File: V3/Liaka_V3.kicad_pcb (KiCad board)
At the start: 4 copper layers, 101.6 x 26.9 mm, 81 parts, among them IC1 XTSD04GLGEAG, J1 Conn_Coaxial, J2 2-3S_LiPo_LARGE_HOLE_XT-30, J3 RRC3_In, J4 I2C_Interface_Male, J5 USB_B_Micro, J7 THD2528-11SD-GF, Q1 Si2301CDS, Q2 Si2301CDS, Q3 Si2301CDS, Q4 MMBT2222, Q5 MMBT2222, Q6 2N7002, SW1 SW_SPDT, SW2 RST, SW3 BOOT, SW4 SD_DUMP, U1 L80-M39, U10 MPU-6050, U2 MS561101BA03-50, U3 ADXL375BCCZ-RL7, U4 RFM95W-915S2, U5 LM393, U6 ADR5040ARTZ-2.048, U7 AMS1117-3.3, U8 CP2102N-A01-GQFN28, U9 ESP32-WROOM-32

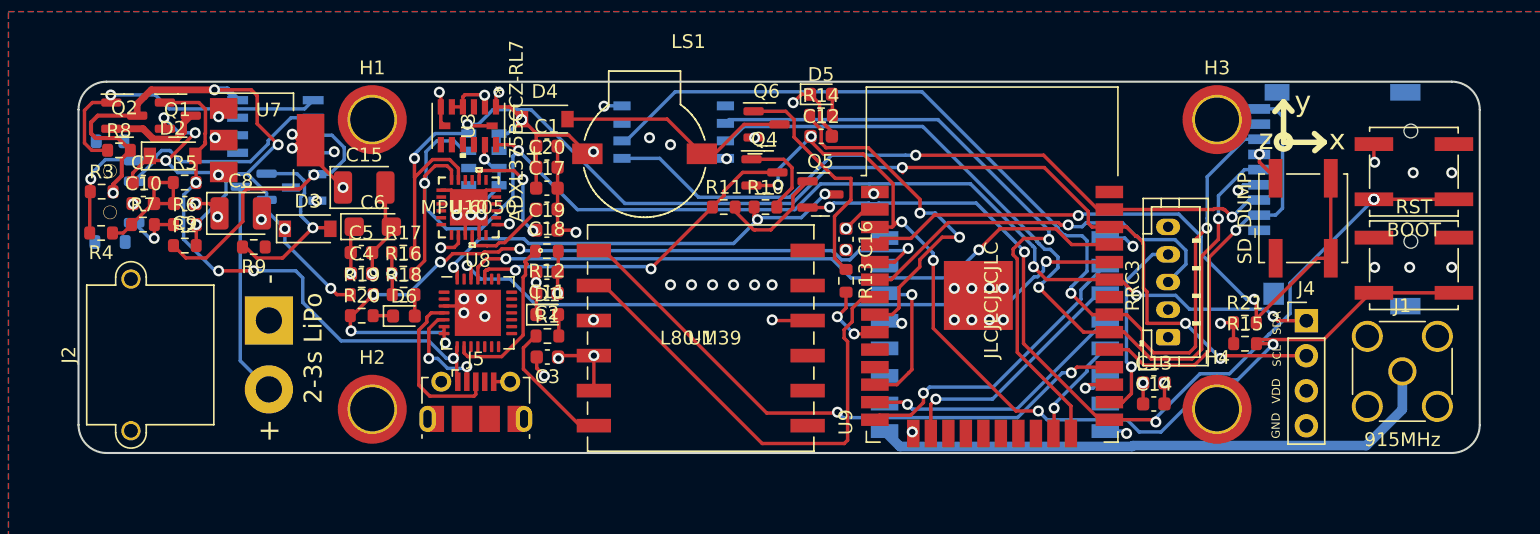
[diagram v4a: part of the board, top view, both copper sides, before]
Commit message: New parts placed and routed
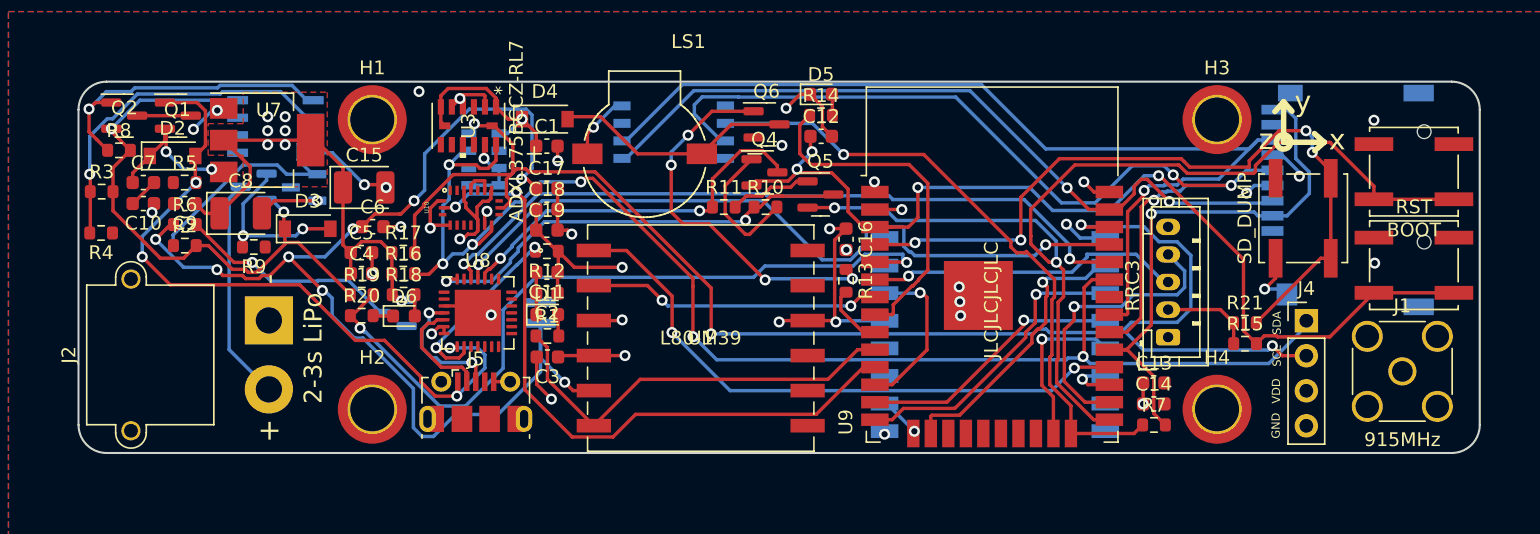
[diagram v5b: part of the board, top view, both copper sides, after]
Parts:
- removed C20: 0.1uF, Capacitor_SMD:C_0603_1608Metric
- removed SW1: SW_SPDT, Local_footprints:SSSS811101
- added BT1: MS621FE-FL11E, Local_footprints:BAT_MS621FE-FL11E, B.Cu at (135.1, 98.0)
- added D7: BAT54C, Package_TO_SOT_SMD:SOT-23, B.Cu at (129.5, 98.0)
- C17: value 10nF -> 4.7u
- C18: value 0.1uF -> 100nF
- C19: value 2.2nF -> 100nF
- C6: value 10uF -> 100n; footprint Capacitor_Tantalum_SMD:CP_EIA-3216-18_Kemet-A -> Capacitor_SMD:C_0603_1608Metric
- R2: value 50k -> 56k
- R6: value 3M -> 1k
- R7: value 1M -> NC
- U10: value MPU-6050 -> BMX055; footprint Local_footprints:MPU-6050 -> Local_footprints:BMX055
- moved R7 74.7 mm to (184.7, 106.2)
- moved J7 0.97 mm to (201.0, 90.1)
- moved U10 0.15 mm to (135.1, 90.4), turned to 90 degrees
- turned C10 to 180 degrees
- turned C18 to 0 degrees
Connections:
- net BOOT renamed /BOOT
- net BUZZER renamed /ESP32/BUZZER
- net Batt_sense renamed /ESP32/Batt_sense
- net CLK_SD renamed /CLK_SD
- net CS_RF renamed /CS_RF
- net DTR renamed /Programming/DTR
- net EN renamed /EN
- net ESP_LED renamed /ESP32/ESP_LED
- net MISO_SD renamed /MISO_SD
- net MOSI_SD renamed /MOSI_SD
- net RESET_RF renamed /RESET_RF
- net RF_IO0 renamed /RF_IO0
- net RTS renamed /Programming/RTS
- net RXD0 renamed /RXD0
- net RXD1_RRC3 renamed /RXD1_RRC3
- net RXD2_GPS renamed /RXD2_GPS
- net SCK_RF renamed /SCK_RF
- net SD_DUMP renamed /SD_DUMP
- net TXD0 renamed /TXD0
- net TXD1_RRC3 renamed /TXD1_RRC3
- net TXD2_GPS renamed /TXD2_GPS
- C17 pad 1: VDD -> /Sensors/V_BKCP
- C18 pad 1: GND -> VDD
- C18 pad 2: Net-(C18-Pad2) -> GND
- C19 pad 1: Net-(C19-Pad1) -> VDD
- C6 pad 1: VDD -> /Sensors/V_BKCP
- IC1 pad 2: CS_XT -> /CS_XT
- J4 pad 1: SDA -> /SDA
- J4 pad 2: SCL -> /SCL
- J7 pad 2: CS_SD -> /CS_SD
- J7 pad 9: CS_SD -> /CS_SD
- J7 pad MP1: unconnected-(J7-PadMP1) -> GND
- J7 pad MP2: unconnected-(J7-PadMP2) -> GND
- J7 pad MP3: unconnected-(J7-PadMP3) -> GND
- J7 pad MP4: unconnected-(J7-PadMP4) -> GND
- Q2 pad 2: VCC -> VDC
- Q2 pad 3: VDC -> VCC
- R1 pad 1: Net-(R1-Pad1) -> /GPS_PPS
- R16 pad 2: SDA -> /SDA
- R17 pad 2: SCL -> /SCL
- R3 pad 1: /Power/2s -> Net-(R3-Pad1)
- R4 pad 2: /Power/2s -> Net-(R3-Pad1)
- R6 pad 1: /Power/3s -> /Sensors/V_BKCP
- R6 pad 2: VDC -> Net-(D7-Pad3)
- R7 pad 1: GND -> /CS_XT
- R7 pad 2: /Power/3s -> /CS_SD
- U1 pad 5: VDD -> /Sensors/V_BKCP
- U1 pad 6: Net-(R1-Pad1) -> /GPS_PPS
- U10 pad 1: GND -> /Sensors/BMX_Int_2
- U10 pad 10: Net-(C18-Pad2) -> /Sensors/BMX_Int_5
- U10 pad 11: GND -> /SDA
- U10 pad 12: unconnected-(U10-Pad12) -> GND
- U10 pad 14: unconnected-(U10-Pad14) -> /Sensors/BMX_Int_3
- U10 pad 15: unconnected-(U10-Pad15) -> /Sensors/BMX_Int_4
- U10 pad 17: unconnected-(U10-Pad17) -> GND
- U10 pad 18: GND -> (no net)
- U10 pad 19: unconnected-(U10-Pad19) -> /BMX_Int_1
- U10 pad 2: unconnected-(U10-Pad2) -> /Sensors/BMX_DRDYM
- U10 pad 20: Net-(C19-Pad1) -> GND
- U10 pad 3: unconnected-(U10-Pad3) -> VDD
- U10 pad 4: unconnected-(U10-Pad4) -> GND
- U10 pad 6: unconnected-(U10-Pad6) -> GND
- U10 pad 7: unconnected-(U10-Pad7) -> VDD
- U10 pad 8: VDD -> (no net)
- U10 pad 9: GND -> /SCL
- U2 pad 7: SDA -> /SDA
- U2 pad 8: SCL -> /SCL
- U3 pad 13: SDA -> /SDA
- U3 pad 14: SCL -> /SCL
- U4 pad 2: MISO_RF -> /MOSI_RF
- U4 pad 3: MOSI_RF -> /MISO_RF
- U5 pad 2: Net-(SW1-Pad2) -> Net-(R3-Pad1)
- U9 pad 10: IO25 -> /GPS_PPS
- U9 pad 11: IO26 -> /BMX_Int_1
- U9 pad 14: MISO_RF -> /MISO_RF
- U9 pad 16: MOSI_RF -> /MOSI_RF
- U9 pad 24: CS_XT -> /CS_XT
- U9 pad 29: CS_SD -> /CS_SD
- U9 pad 33: SDA -> /SDA
- U9 pad 36: SCL -> /SCL
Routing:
- net /SCL: track 0.00 -> 107.2 mm, vias 0 -> 4
- net /SDA: track 0.00 -> 100.8 mm, vias 0 -> 6
- net SDA: track 96.3 -> 0.00 mm, vias 5 -> 0
- net SCL: track 94.2 -> 0.00 mm, vias 5 -> 0
- net /Sensors/V_BKCP: track 0.00 -> 82.2 mm, vias 0 -> 8
- net /BMX_Int_1: track 0.00 -> 49.3 mm, vias 0 -> 2
- net /CS_XT: track 0.00 -> 46.2 mm, vias 0 -> 1
- net CS_XT: track 45.6 -> 0.00 mm, vias 1 -> 0
- net VDD: track 63.1 -> 108.2 mm, vias 27 -> 20
- net /CS_SD: track 0.00 -> 38.8 mm, vias 0 -> 1
- net /GPS_PPS: track 0.00 -> 30.9 mm
- net CS_SD: track 30.3 -> 0.00 mm, vias 1 -> 0
- net Net-(R3-Pad1): track 0.00 -> 25.4 mm, vias 0 -> 1
- net MISO_RF: track 22.1 -> 0.00 mm, vias 1 -> 0
- net /MISO_RF: track 0.00 -> 21.9 mm, vias 0 -> 1
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- added copper zone on F.Cu, net VDD
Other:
- board text added: "Designed by Angus McLennan October 2022"
- board text removed: "2s"
- board text removed: "3s"
- board text removed: "Designed by Angus McLennan March 2022"
